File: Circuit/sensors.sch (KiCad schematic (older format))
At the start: 6 parts, among them U301 BME280, U302 ADXL345

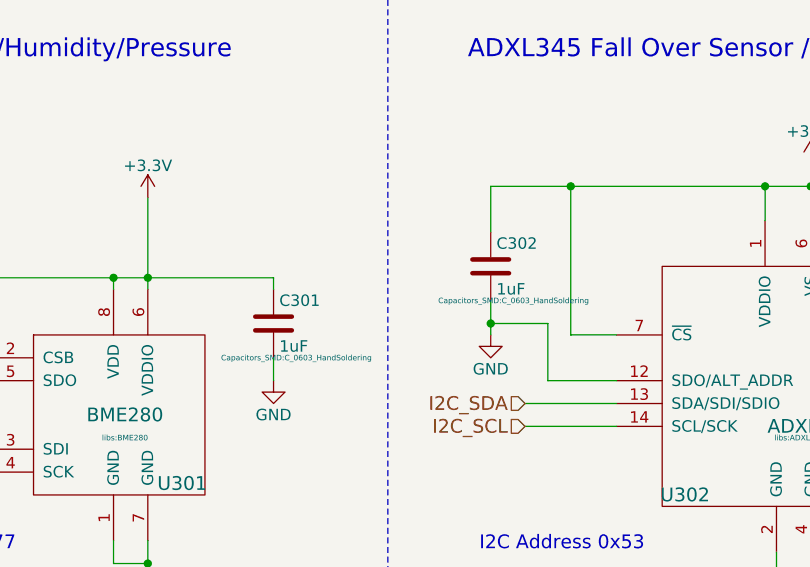
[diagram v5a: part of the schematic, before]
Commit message: Changes for BOM generation. Corrections to redundant BOM items.
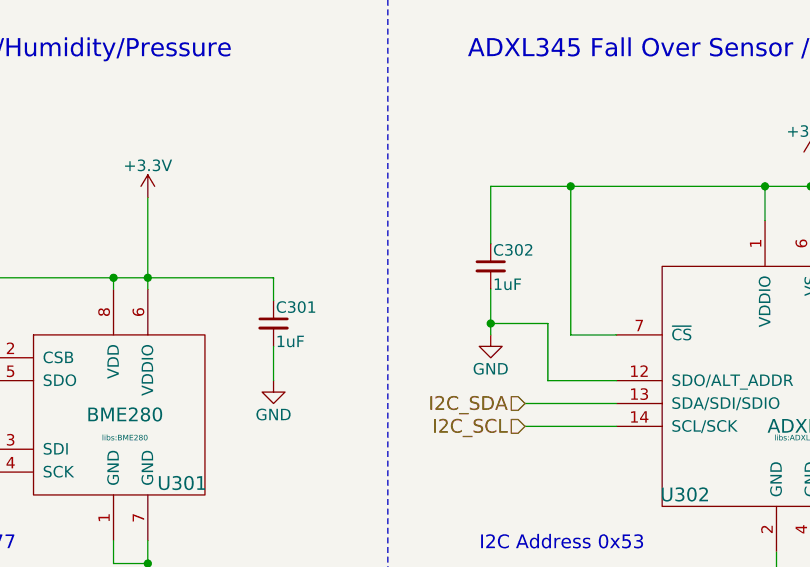
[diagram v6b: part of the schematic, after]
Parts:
- removed C301, C302: 1uF, Capacitors_SMD:C_0603_HandSoldering, symbol C
- added C301, C302: 1uF, Capacitors_SMD:C_0603_HandSoldering, symbol C_Small
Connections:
- net +3V3: now also C301.1, C302.1
- net GND: now also C301.2, C302.2
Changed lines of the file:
@@
 NoConn ~ 7100 2950
 Wire Wire Line
-	4750 2800 4750 2950
+	4750 2750 4750 2950
 $Comp
 L GND #PWR047
@@
 $EndComp
 Wire Wire Line
-	4750 2500 4750 2300
+	4750 2300 4750 2550
 Connection ~ 5100 2300
-$Comp
-L C C301
-U 1 1 564CEC68
-P 3800 2900
-F 0 "C301" H 3825 3000 50  0000 L CNN
-F 1 "1uF" H 3825 2800 50  0000 L CNN
-F 2 "Capacitors_SMD:C_0603_HandSoldering" H 3900 2750 24  0000 C CNN
-F 3 "" H 3800 2900 60  0000 C CNN
-F 4 "311-1372-1-ND" H 3800 2900 60  0001 C CNN "Digikey PN"
-F 5 "http://www.digikey.com.au/product-detail/en/yageo/CC0603ZRY5V7BB105/311-1372-1-ND/2103156" H 3800 2900 60  0001 C CNN "Link"
-F 6 "CC0603ZRY5V7BB105" H 3800 2900 60  0001 C CNN "Manufacturer PN"
-F 7 "0.10" H 3800 2900 60  0001 C CNN "Unit Cost"
-	1    3800 2900
-	1    0    0    -1
-$EndComp
 Wire Wire Line
-	3800 2700 3800 2750
+	3800 2700 3800 2800
 Wire Wire Line
-	3800 3050 3800 3150
+	3800 3000 3800 3150
 $Comp
 L GND #PWR048
@@
 $EndComp
 $Comp
-L C C302
-U 1 1 58232438
+L C_Small C302
+U 1 1 5847A71A
 P 4750 2650
-F 0 "C302" H 4775 2750 50  0000 L CNN
-F 1 "1uF" H 4775 2550 50  0000 L CNN
-F 2 "Capacitors_SMD:C_0603_HandSoldering" H 4850 2500 24  0000 C CNN
-F 3 "" H 4750 2650 60  0000 C CNN
-F 4 "311-1372-1-ND" H 4750 2650 60  0001 C CNN "Digikey PN"
-F 5 "http://www.digikey.com.au/product-detail/en/yageo/CC0603ZRY5V7BB105/311-1372-1-ND/2103156" H 4750 2650 60  0001 C CNN "Link"
-F 6 "CC0603ZRY5V7BB105" H 4750 2650 60  0001 C CNN "Manufacturer PN"
-F 7 "0.10" H 4750 2650 60  0001 C CNN "Unit Cost"
+F 0 "C302" H 4760 2720 50  0000 L CNN
+F 1 "1uF" H 4760 2570 50  0000 L CNN
+F 2 "Capacitors_SMD:C_0603_HandSoldering" H 4750 2650 50  0001 C CNN
+F 3 "" H 4750 2650 50  0000 C CNN
+F 4 "490-1536-1-ND" H 4750 2650 60  0001 C CNN "Digikey PN"
+F 5 "http://www.digikey.com.au/product-detail/en/murata-electronics-north-america/GRM188R61C105KA93D/490-1536-1-ND/587769" H 4750 2650 60  0001 C CNN "Link"
+F 6 "GRM188R61C105KA93D" H 4750 2650 60  0001 C CNN "Manufacturer PN"
+F 7 "0.1" H 4750 2650 60  0001 C CNN "Unit Cost"
 	1    4750 2650
 	1    0    0    -1
 $EndComp
+$Comp
+L C_Small C301
+U 1 1 5847A76F
+P 3800 2900
+F 0 "C301" H 3810 2970 50  0000 L CNN
+F 1 "1uF" H 3810 2820 50  0000 L CNN
+F 2 "Capacitors_SMD:C_0603_HandSoldering" H 3800 2900 50  0001 C CNN
+F 3 "" H 3800 2900 50  0000 C CNN
+F 4 "490-1536-1-ND" H 3800 2900 60  0001 C CNN "Digikey PN"
+F 5 "http://www.digikey.com.au/product-detail/en/murata-electronics-north-america/GRM188R61C105KA93D/490-1536-1-ND/587769" H 3800 2900 60  0001 C CNN "Link"
+F 6 "GRM188R61C105KA93D" H 3800 2900 60  0001 C CNN "Manufacturer PN"
+F 7 "0.1" H 3800 2900 60  0001 C CNN "Unit Cost"
+	1    3800 2900
+	1    0    0    -1
+$EndComp
